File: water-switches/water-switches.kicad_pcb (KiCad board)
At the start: 2 copper layers, 55.9 x 20.3 mm, 27 parts, among them J1 PWR, J10 Out4, J11 In4, J12 Out5, J13 In5, J2 Out0, J3 In0, J4 Out1, J5 IN1, J6 Out2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

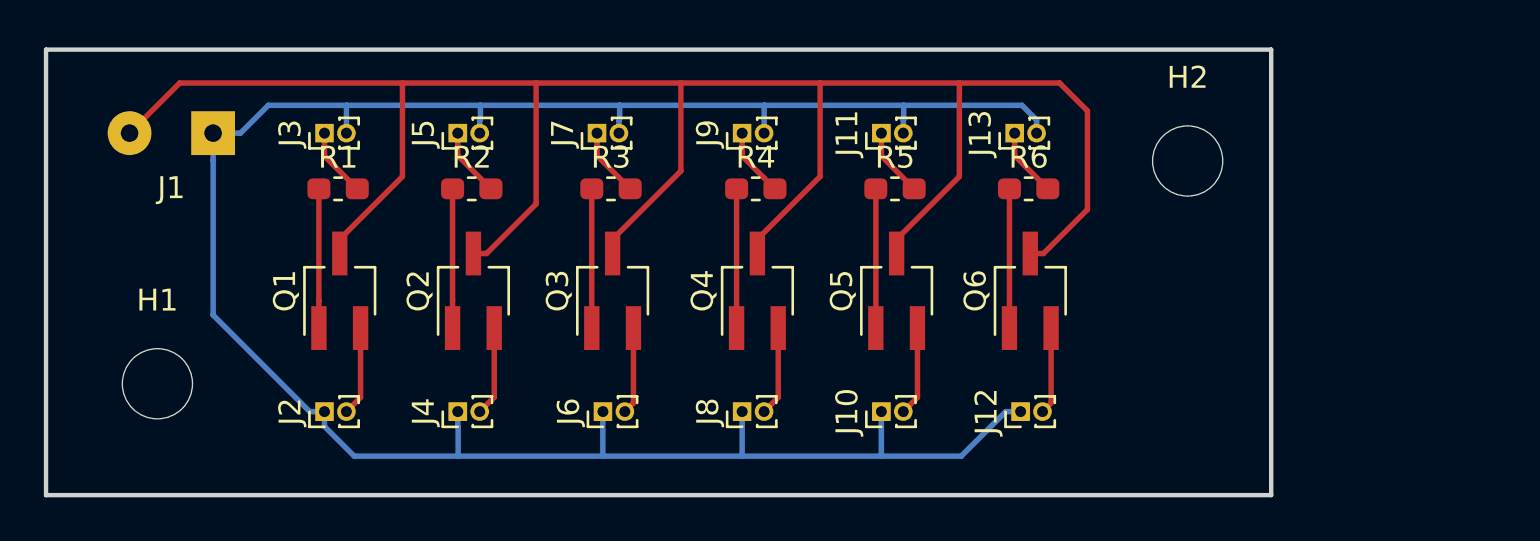
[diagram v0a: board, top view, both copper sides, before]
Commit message: Add relay to water-switches
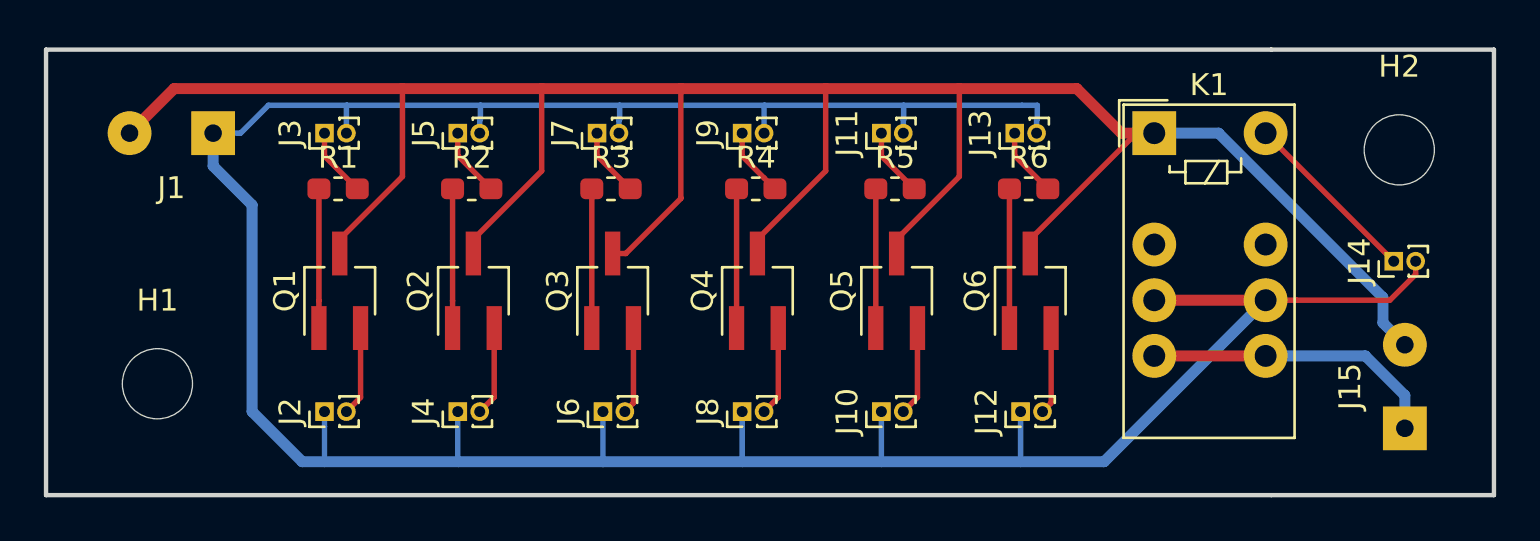
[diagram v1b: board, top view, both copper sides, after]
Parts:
- added J14: In6, Connector_PinHeader_1.00mm:PinHeader_1x02_P1.00mm_Vertical, F.Cu at (158.0, 80.8)
- added J15: Out6, Connector_Wire:SolderWirePad_1x02_P3.81mm_Drill0.8mm, F.Cu at (158.5, 88.4)
- added K1: G6S-2, Relay_THT:Relay_DPDT_Omron_G6S-2, F.Cu at (147.1, 74.9)
- moved H2 9.67 mm to (158.2, 75.7)
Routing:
- net +12V: track 102.5 -> 136.2 mm
- net GND: track 98.4 -> 117.0 mm
- net Net-(J15-Pad1): track 0.00 -> 13.7 mm
- net Net-(J14-Pad1): track 0.00 -> 8.26 mm
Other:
- board size 55.9 x 20.3 mm -> 66 x 20.3 mm
